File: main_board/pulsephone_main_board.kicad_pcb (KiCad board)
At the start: 4 copper layers, 70.5 x 128.5 mm, 47 parts, among them J1 USB_C_Receptacle_USB2.0_14P, J2 Conn_01x05, J3 Conn_2Rows-35Pins_MountingPin, J4 Conn_2Rows-35Pins_MountingPin, J5 Conn_2Rows-35Pins_MountingPin, SW1 SW_DPST_x2, U1 XL1509-3.3, U2 PCM5102APWR, U5 TP4056-42-ESOP8

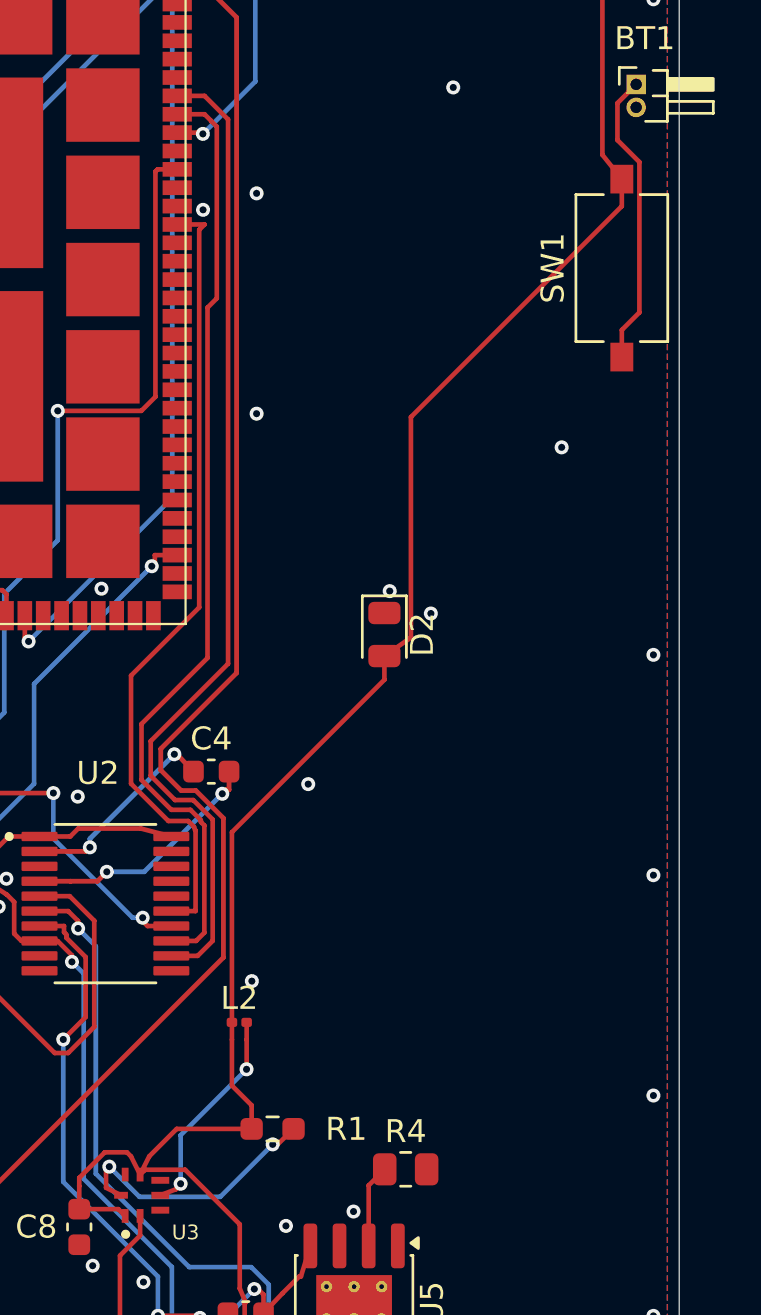
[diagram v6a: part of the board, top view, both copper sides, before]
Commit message: remove battery switch
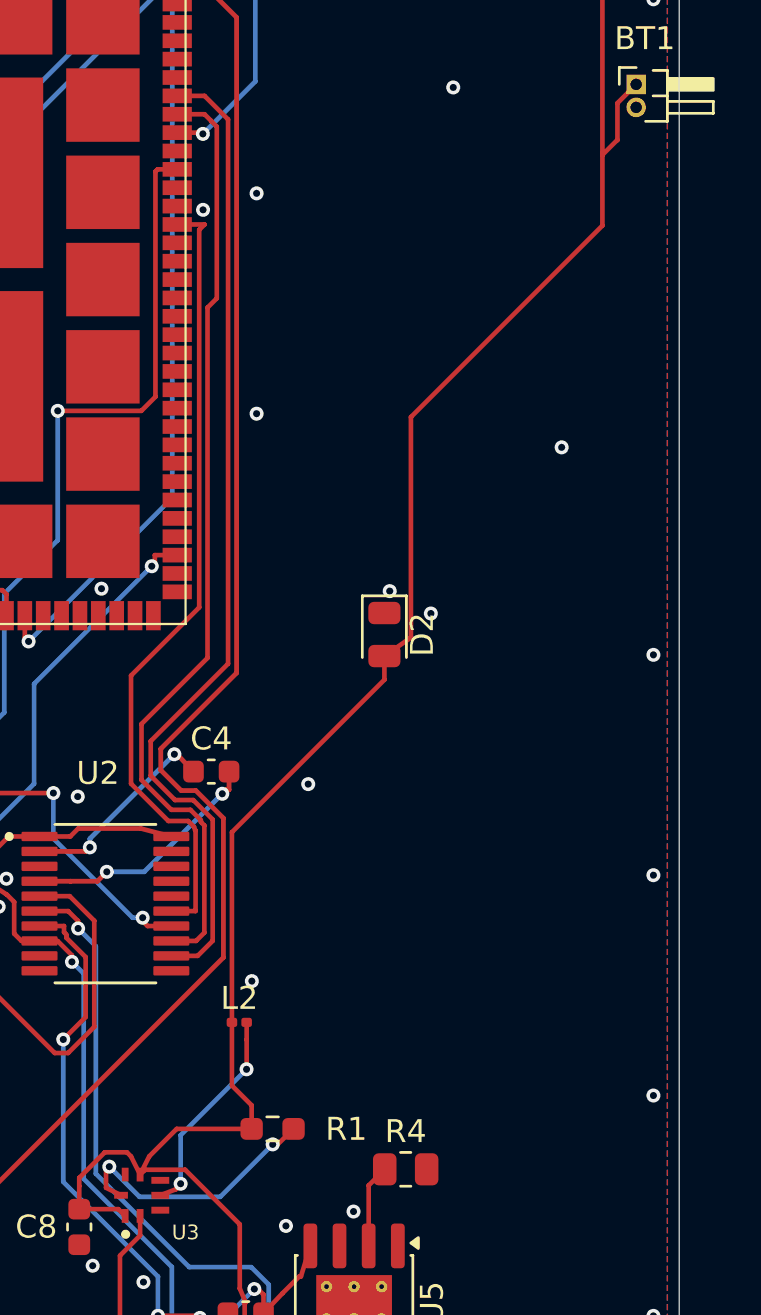
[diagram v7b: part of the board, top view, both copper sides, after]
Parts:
- removed SW1: SW_DPST_x2, Button_Switch_SMD:SW_Tactile_SPST_NO_Straight_CK_PTS636Sx25SMTRLFS
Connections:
- BT1 pad 1: Net-(BT1-+) -> +3.7VBAT
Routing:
- net Net-(BT1-+): track 12.9 -> 0.00 mm
- net +3.7VBAT: track 250.8 -> 253.9 mm

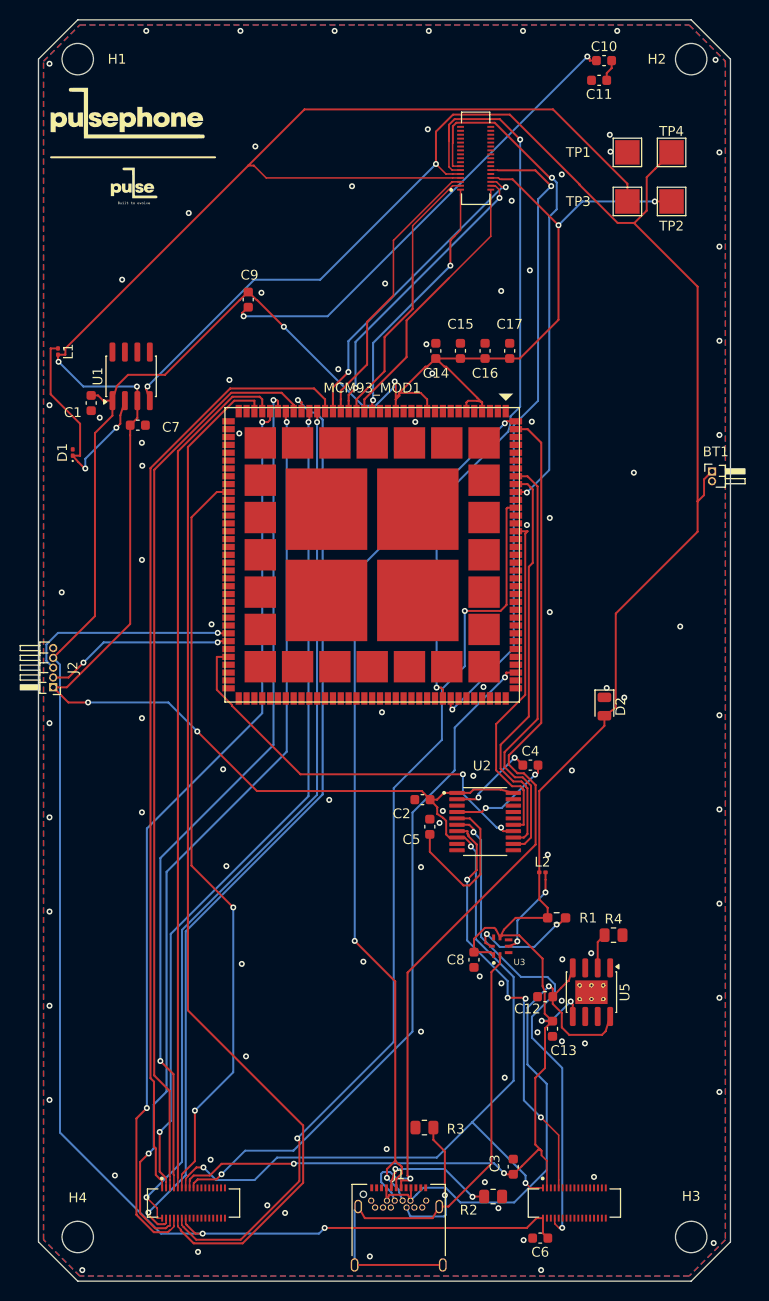
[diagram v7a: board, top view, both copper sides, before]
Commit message: add sd card slot. also add rst and onoff buttons
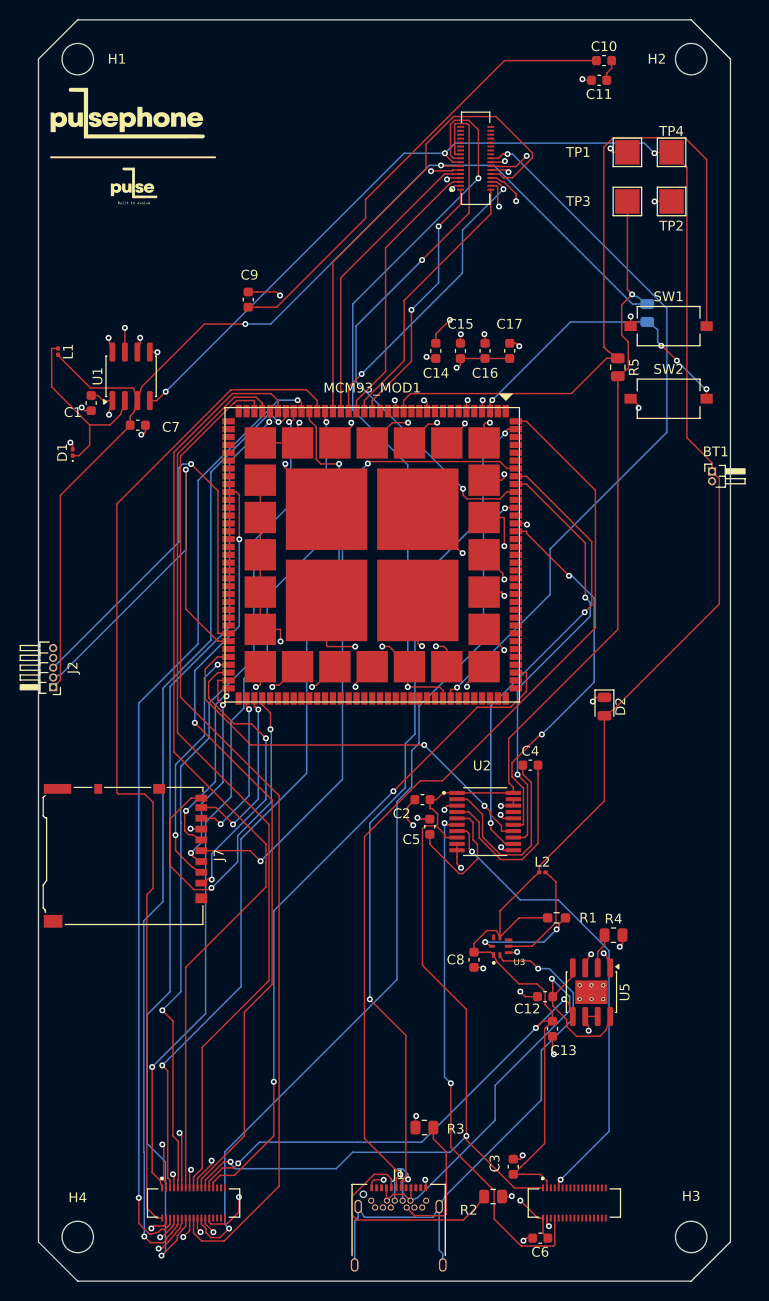
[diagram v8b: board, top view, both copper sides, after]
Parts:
- added J7: Micro_SD_Card_Det1, Connector_Card:microSD_HC_Hirose_DM3AT-SF-PEJM5, F.Cu at (109.9, 111.2)
- added R5: 10 kΩ, Resistor_SMD:R_0805_2012Metric, F.Cu at (160.0, 61.4)
- added R6: 10 kΩ, Resistor_SMD:R_0805_2012Metric, B.Cu at (163.0, 55.9)
- added SW1: SW_Push, Button_Switch_SMD:SW_Tactile_SPST_NO_Straight_CK_PTS636Sx25SMTRLFS, F.Cu at (165.2, 57.2)
- added SW2: SW_Push, Button_Switch_SMD:SW_Tactile_SPST_NO_Straight_CK_PTS636Sx25SMTRLFS, F.Cu at (165.2, 64.6)
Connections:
- MCM93_MOD1 pad 134: unconnected-(MCM93_MOD1D-29-Pad134) -> SD2_VDD
- MCM93_MOD1 pad 14: unconnected-(MCM93_MOD1-Pad14) -> RESET
- MCM93_MOD1 pad 3: unconnected-(MCM93_MOD1-Pad3) -> ONOFF
- MCM93_MOD1 pad 65: unconnected-(MCM93_MOD1B-30-Pad65) -> SD2_RST_B
- MCM93_MOD1 pad 67: unconnected-(MCM93_MOD1B-32-Pad67) -> SD2_DAT3
- MCM93_MOD1 pad 68: unconnected-(MCM93_MOD1B-33-Pad68) -> SD2_DAT2
- MCM93_MOD1 pad 69: unconnected-(MCM93_MOD1B-34-Pad69) -> SD2_CMD
- MCM93_MOD1 pad 70: unconnected-(MCM93_MOD1B-35-Pad70) -> SD2_CLK
- MCM93_MOD1 pad 72: unconnected-(MCM93_MOD1C-2-Pad72) -> SD2_DAT0
- MCM93_MOD1 pad 73: unconnected-(MCM93_MOD1C-3-Pad73) -> SD2_DAT1
- MCM93_MOD1 pad 74: unconnected-(MCM93_MOD1C-4-Pad74) -> SD2_CD_B
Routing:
- net +5V: track 248.1 -> 32.2 mm, vias 6 -> 12
- net GND: track 0.00 -> 213.5 mm, vias 96 -> 81
- net RESET: track 0.00 -> 75.7 mm
- net SD2_VDD: track 0.00 -> 67.0 mm, vias 0 -> 2
- net SD2_CD_B: track 0.00 -> 36.3 mm, vias 0 -> 2
- net ONOFF: track 0.00 -> 30.8 mm, vias 0 -> 4
- net SD2_DAT2: track 0.00 -> 29.5 mm, vias 0 -> 2
- net UART_RX: track 19.4 -> 46.9 mm, vias 2 -> 1
- net SD2_DAT3: track 0.00 -> 25.3 mm, vias 0 -> 2
- net UART_TX: track 21.7 -> 46.5 mm
- net SD2_CMD: track 0.00 -> 21.7 mm, vias 0 -> 2
- net SD2_CLK: track 0.00 -> 18.5 mm, vias 0 -> 2
- net /CSI_D1_P: track 32.1 -> 50.4 mm, vias 2 -> 0
- net SD2_DAT1: track 0.00 -> 18.1 mm, vias 0 -> 2
- net SD2_DAT0: track 0.00 -> 16.3 mm, vias 0 -> 2
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- added copper zone on In2.Cu, net +5V
- removed copper zone on B.Cu, net GND
- removed copper zone on F.Cu, net GND
- removed copper zone on In2.Cu, net GND
